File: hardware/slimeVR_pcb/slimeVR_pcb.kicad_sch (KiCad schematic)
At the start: 43 parts, among them J1 USB_C_Receptacle_USB2.0_16P, Q1 Q_Dual_NMOS_S1G1S2G2D2D2D1D1, SW1 SW_SPDT, SW3 SW_Push, U1 ESP32-S2-WROVER, U10 AP2112K-3.3, U2 TP4057, U3 ICM-45686, U5 QMC6309, U6 TPS25200DRVR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

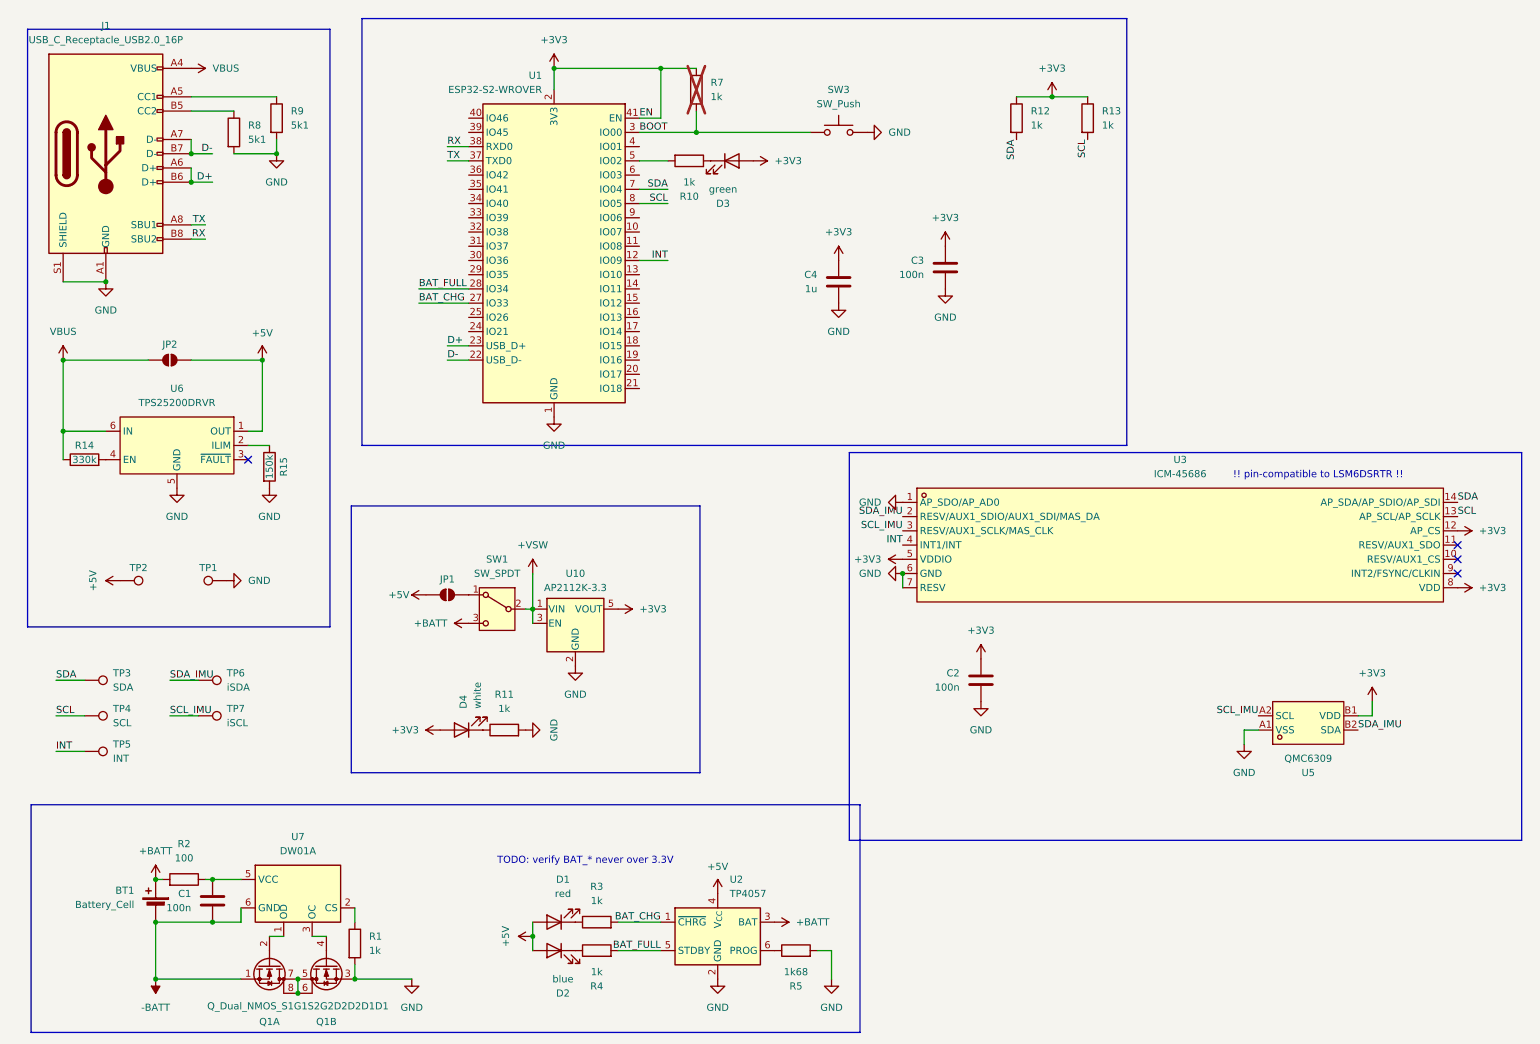
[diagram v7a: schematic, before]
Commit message: more testpad
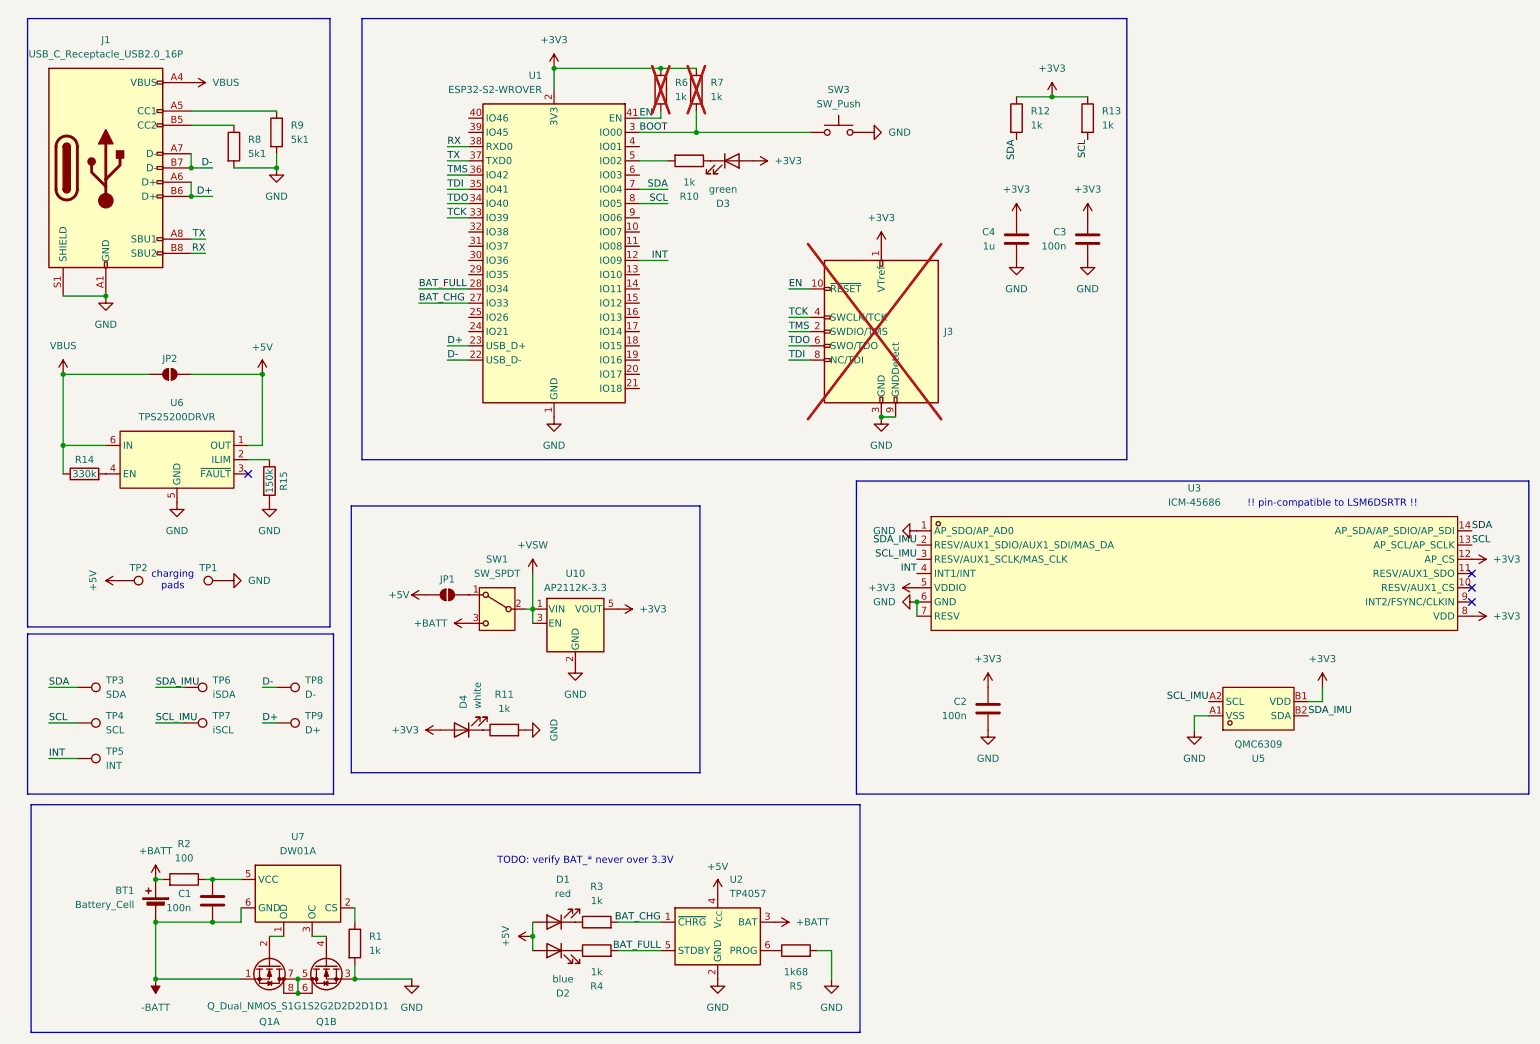
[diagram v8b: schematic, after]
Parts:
- added J3: Conn_ARM_JTAG_SWD_10, Connector:Tag-Connect_TC2050-IDC-NL_2x05_P1.27mm_Vertical, symbol Connector:Conn_ARM_JTAG_SWD_10
- added R6: 1k, Resistor_SMD:R_0603_1608Metric_Pad0.98x0.95mm_HandSolder, symbol Device:R
- added TP8: D-, TestPoint:TestPoint_Pad_D1.0mm, symbol Connector:TestPoint
- added TP9: D+, TestPoint:TestPoint_Pad_D1.0mm, symbol Connector:TestPoint
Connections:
- net +3V3: now also J3.1 (VTref), R6.1; no longer U1.41 (EN)
- net D+: now also TP9.1
- net D-: now also TP8.1
- net GND: now also J3.3 (GND), J3.5 (GND), J3.9 (GNDDetect)
- net TCK: now reaches U1.33 (IO39)
- net TCK: now also J3.4 (SWCLK/TCK)
- net TDO: now reaches U1.34 (IO40)
- net TDO: now also J3.6 (SWO/TDO)
- net TDI: now reaches U1.35 (IO41)
- net TDI: now also J3.8 (NC/TDI)
- net TMS: now reaches U1.36 (IO42)
- net TMS: now also J3.2 (SWDIO/TMS)
- new net EN: J3.10 (~{RESET}), R6.2, U1.41 (EN)
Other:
- note added: "charging pads"
- moved on the sheet: C2, C3, C4, J1, JP2, R14, R15, R8, R9, TP3, TP4, TP5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
